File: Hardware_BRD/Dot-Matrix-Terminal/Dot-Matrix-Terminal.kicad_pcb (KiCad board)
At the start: 2 copper layers, 105 x 50 mm, 62 parts, among them J1 USB_B, J2 Conn_01x17, J3 Conn_01x10, J4 Conn_01x02, J5 Barrel_Jack, J6 Conn_01x02, J7 Conn_01x02, J8 Conn_01x02, Q1 IRLML0030, Q10 IRLML0030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

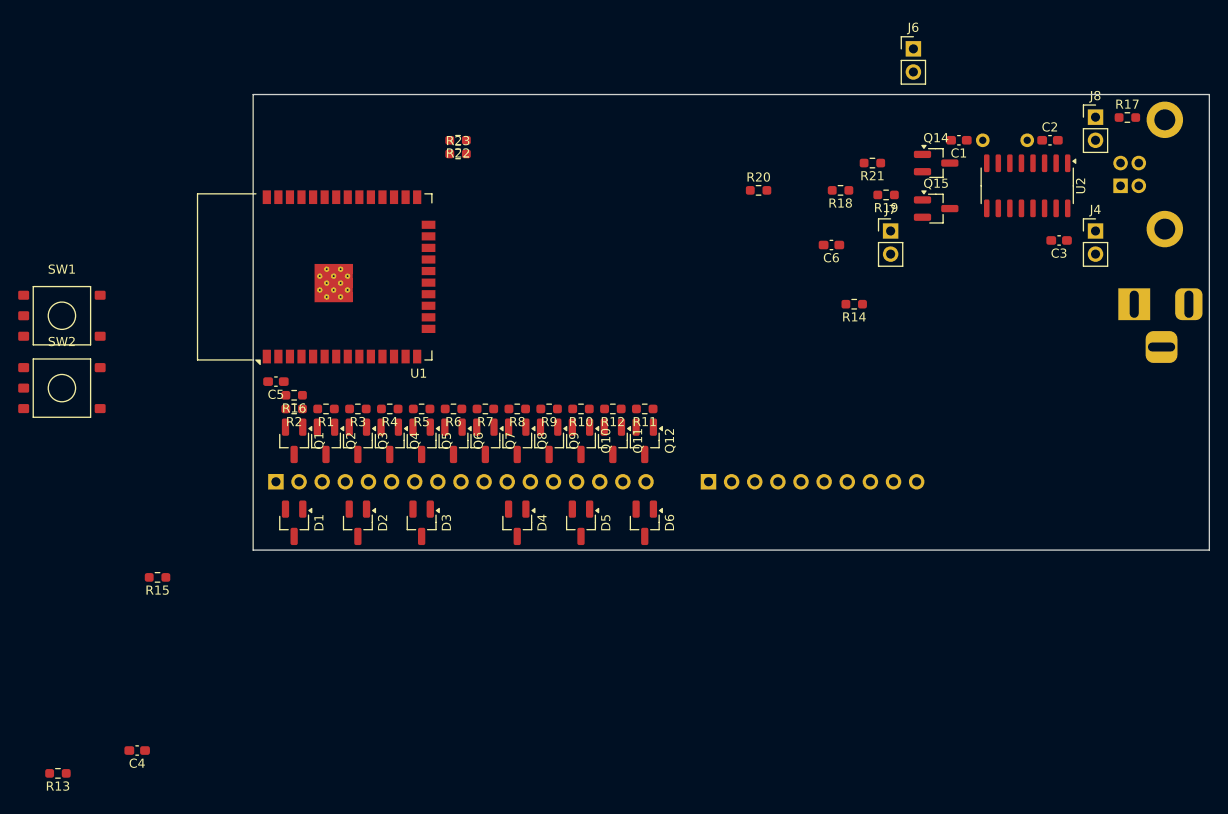
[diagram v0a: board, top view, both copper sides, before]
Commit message: unsuccessful attempt at single layer routing
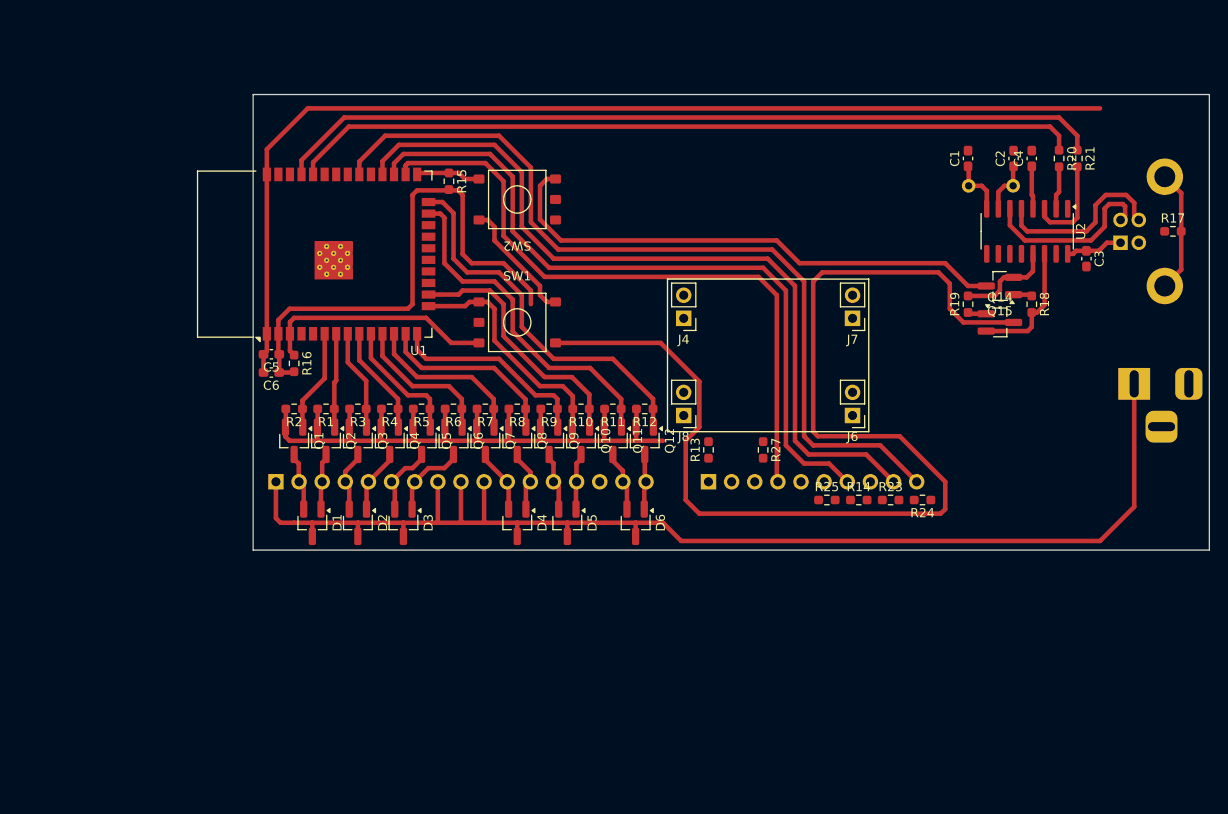
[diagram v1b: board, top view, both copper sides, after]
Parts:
- removed R22: 10k, Resistor_SMD:R_0603_1608Metric_Pad0.98x0.95mm_HandSolder
- added R24: 10k, Resistor_SMD:R_0603_1608Metric_Pad0.98x0.95mm_HandSolder, F.Cu at (173.5, 144.5)
- added R25: 10k, Resistor_SMD:R_0603_1608Metric_Pad0.98x0.95mm_HandSolder, F.Cu at (163.0, 144.5)
- added R27: 10k, Resistor_SMD:R_0603_1608Metric_Pad0.98x0.95mm_HandSolder, F.Cu at (156.0, 139.0)
- moved C4 117.8 mm to (185.5, 107.0), turned to 90 degrees
- moved R13 79.8 mm to (150.0, 139.0), turned to 90 degrees
- moved C6 63.1 mm to (102.0, 130.5)
- moved R23 60.8 mm to (170.0, 144.5)
- moved J8 55.8 mm to (147.3, 135.2), turned to 180 degrees
- moved SW2 54.1 mm to (129.0, 111.5), turned to 180 degrees
- moved R15 54.0 mm to (121.5, 109.5), turned to -90 degrees
- moved SW1 50.0 mm to (129.0, 125.0)
- moved J4 46.2 mm to (147.3, 124.6), turned to 180 degrees
- moved J6 40.8 mm to (165.8, 135.2), turned to 180 degrees
- moved R20 33.2 mm to (188.5, 107.0), turned to -90 degrees
- moved R18 24.4 mm to (185.5, 123.0), turned to -90 degrees
- moved R21 22.5 mm to (190.5, 107.0), turned to -90 degrees
- moved R14 21.5 mm to (166.5, 144.5), turned to 0 degrees
- moved Q14 18.8 mm to (182.0, 125.0)
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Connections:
- J3 pad 6: /INDEX_SNS -> unconnected-(J3-Pin_6-Pad6)
- J4 pad 1: +24V -> +3.3V
- J4 pad 2: +24V -> +3.3V
- J7 pad 1: +3.3V -> +24V
- J7 pad 2: +3.3V -> +24V
- Q11 pad 1: /FEED_R -> /FEED_L
- R11 pad 1: /FEED_R -> /FEED_L
- R15 pad 1: +3.3V -> Net-(Q15-C)
- R15 pad 2: Net-(Q15-C) -> +3.3V
- R23 pad 1: Net-(U1-IO2) -> +3.3V
- R23 pad 2: GND -> /FEED_L_SNS
- U1 pad 13: /FEED_R_SNS -> /PIN5
- U1 pad 14: /LINE_SNS -> /PIN3
- U1 pad 16: /FEED_L_SNS -> /PIN1
- U1 pad 23: /INDEX_SNS -> /FEED_L
- U1 pad 24: /PIN3 -> /FEED_R
- U1 pad 27: /PIN5 -> /LINE_SNS
- U1 pad 28: /FEED_R -> /FEED_L_SNS
- U1 pad 29: Net-(U1-IO5) -> unconnected-(U1-IO5-Pad29)
- U1 pad 30: /FEED_R -> /FEED_R_SNS
- U1 pad 31: /PIN1 -> unconnected-(U1-IO19-Pad31)
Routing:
- net GND: track 0.00 -> 239.0 mm
- net Net-(Q14-C): track 0.00 -> 149.0 mm
- net +24V: track 0.00 -> 137.0 mm
- net /FEED_R_SNS: track 0.00 -> 93.0 mm
- net Net-(U1-TXD0/IO1): track 0.00 -> 91.1 mm
- net /FEED_L_SNS: track 0.00 -> 87.1 mm
- net Net-(U1-RXD0/IO3): track 0.00 -> 86.9 mm
- net /LINE_SNS: track 0.00 -> 79.8 mm
- net /FINE_SNS: track 0.00 -> 71.9 mm
- net Net-(Q15-C): track 0.00 -> 64.9 mm
- net +3.3V: track 0.00 -> 58.0 mm
- net /FEED_R: track 0.00 -> 41.7 mm
- net /FEED_L: track 0.00 -> 37.7 mm
- net /PIN1: track 0.00 -> 28.2 mm
- net /PIN3: track 0.00 -> 22.5 mm
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
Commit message: MVP board
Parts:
- removed R23, R24, R25, R27: 10k, Resistor_SMD:R_0603_1608Metric_Pad0.98x0.95mm_HandSolder
- added C7: 1000u, Capacitor_THT:C_Radial_D16.0mm_H25.0mm_P7.50mm, F.Cu at (183.5, 143.8)
- added C8: 1000u, Capacitor_THT:C_Radial_D16.0mm_H25.0mm_P7.50mm, F.Cu at (147.0, 143.8)
- moved R15 30.9 mm to (145.0, 129.5)
- moved Q14 28.2 mm to (157.5, 111.0), turned to 180 degrees
- moved Q15 25.2 mm to (157.5, 115.0)
- moved J6 25.0 mm to (142.4, 126.5)
- moved J7 25.0 mm to (142.4, 115.8)
- moved J4 25.0 mm to (123.9, 115.8)
- moved J8 25.0 mm to (123.9, 126.5)
- moved SW1 24.5 mm to (148.0, 109.5), turned to 90 degrees
- moved R18 24.2 mm to (163.5, 113.0), turned to 90 degrees
- moved R21 22.4 mm to (170.5, 117.0), turned to 0 degrees
- moved R20 21.6 mm to (170.5, 119.0), turned to 0 degrees
- moved R14 20.9 mm to (152.0, 129.5), turned to 90 degrees
- moved SW2 20.8 mm to (148.0, 120.0), turned to 90 degrees
- moved R19 19.7 mm to (161.5, 113.0), turned to -90 degrees
- moved C1 18.8 mm to (186.5, 124.0), turned to -90 degrees
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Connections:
- J3 pad 10: /FEED_R_SNS -> unconnected-(J3-Pin_10-Pad10)
- J3 pad 9: /FEED_L_SNS -> unconnected-(J3-Pin_9-Pad9)
- J4 pad 1: +3.3V -> GND
- J4 pad 2: +3.3V -> GND
- J6 pad 1: GND -> +24V
- J6 pad 2: GND -> +24V
- J7 pad 1: +24V -> GND
- J7 pad 2: +24V -> GND
- J8 pad 1: GND -> +3.3V
- J8 pad 2: GND -> +3.3V
- U1 pad 10: /PIN2 -> /PIN6
- U1 pad 11: /PIN4 -> /PIN9
- U1 pad 12: /PIN7 -> /PIN2
- U1 pad 13: /PIN5 -> /PIN4
- U1 pad 14: /PIN3 -> /PIN7
- U1 pad 16: /PIN1 -> /PIN5
- U1 pad 23: /FEED_L -> /PIN3
- U1 pad 24: /FEED_R -> /PIN1
- U1 pad 26: /FINE_SNS -> /FEED_L
- U1 pad 27: /LINE_SNS -> /FEED_R
- U1 pad 28: /FEED_L_SNS -> /FINE_SNS
- U1 pad 30: /FEED_R_SNS -> /LINE_SNS
- U1 pad 6: /MOTOR -> unconnected-(U1-IO34-Pad6)
- U1 pad 7: /PIN8 -> unconnected-(U1-IO35-Pad7)
- U1 pad 8: /PIN6 -> /MOTOR
- U1 pad 9: /PIN9 -> /PIN8
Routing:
- net /FEED_R_SNS: track 93.0 -> 0.00 mm
- net GND: track 239.0 -> 149.0 mm
- net /FEED_L_SNS: track 87.1 -> 0.00 mm
- net Net-(Q14-C): track 149.0 -> 92.6 mm, vias 0 -> 4
- net +24V: track 137.0 -> 94.4 mm, vias 0 -> 2
- net /FEED_L: track 37.7 -> 71.5 mm
- net /FEED_R: track 41.7 -> 72.8 mm
- net Net-(J3-Pin_8): track 0.00 -> 28.1 mm, vias 0 -> 2
- net Net-(J1-VBUS): track 6.31 -> 31.7 mm
- net Net-(Q15-E): track 10.7 -> 33.5 mm
- net Net-(U1-TXD0/IO1): track 91.1 -> 73.2 mm
- net Net-(J3-Pin_1): track 0.00 -> 16.0 mm, vias 0 -> 2
- net Net-(U1-RXD0/IO3): track 86.9 -> 71.3 mm
- net Net-(Q14-E): track 14.1 -> 23.8 mm
- net /PIN3: track 22.5 -> 29.4 mm
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- added copper zone on F.Cu, net +24V
- added copper zone on F.Cu, net GND
